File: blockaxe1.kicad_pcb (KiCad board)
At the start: 4 copper layers, 56.5 x 99.8 mm, 149 parts, among them J1 TC2030-IDC, J2 TC2030-IDC, J3 Conn_01x04, J4 USB_C_Receptacle_USB2.0, J5 PJ-002B, J6 Conn_01x04, J7 Conn_01x03, Q4 CSD17575Q3, Q5 CSD17312Q5, SW1 TL3330AF260QG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

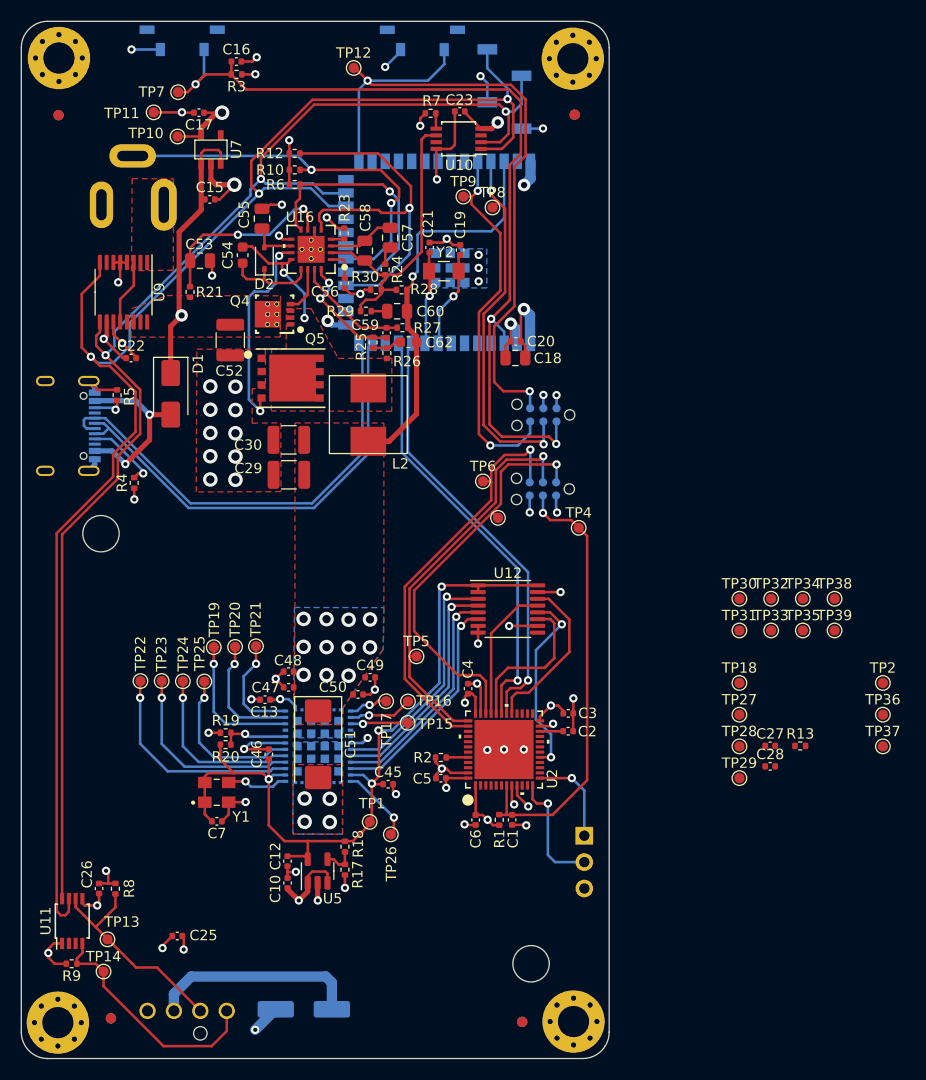
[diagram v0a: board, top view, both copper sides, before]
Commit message: switched barrel plug for #8. touched up schematic, DRC, generated BOM, generated Gerbers
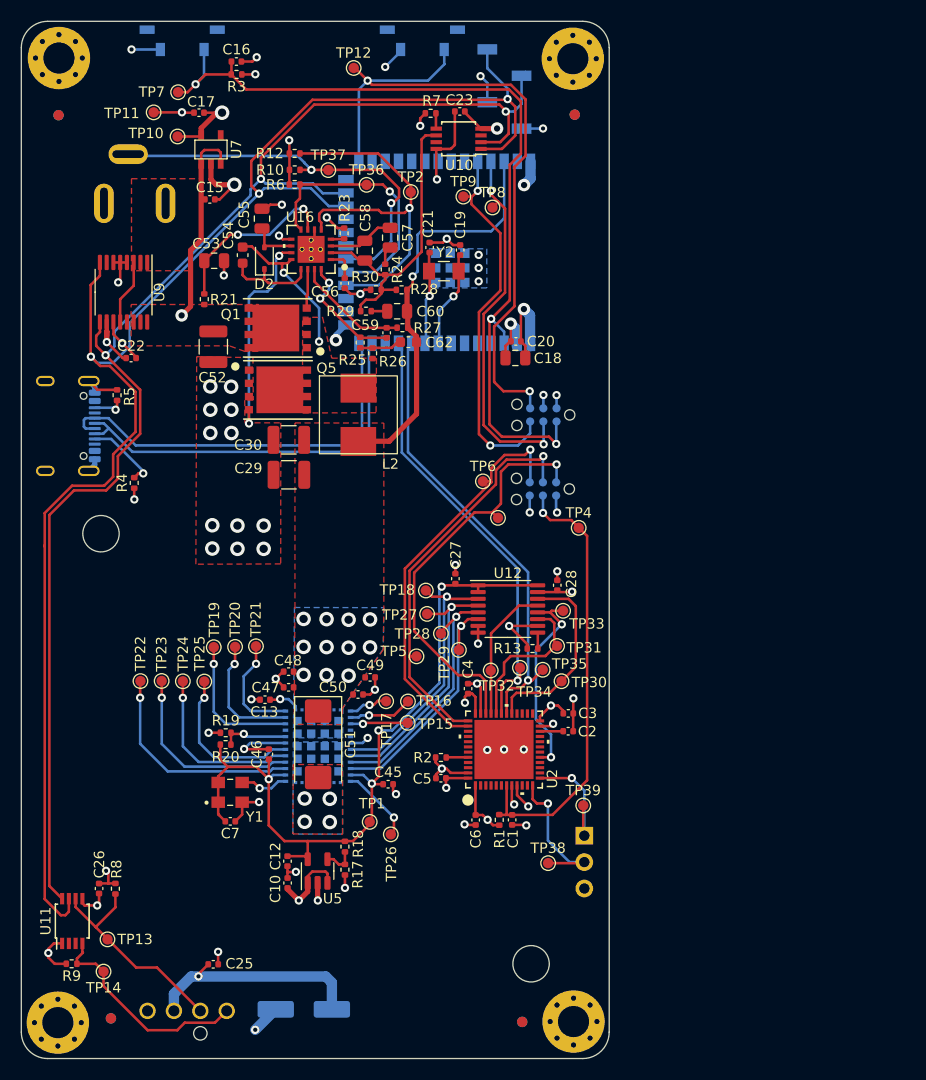
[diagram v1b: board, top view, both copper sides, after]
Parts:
- removed D1: SS310, Diode_SMD:D_SMA
- removed Q4: CSD17575Q3, blockaxe:DQG0008A
- added Q1: CSD17312Q5, blockaxe:DQH8, F.Cu at (128.4, 76.1)
- J5: value PJ-002B -> EJ503A; footprint blockaxe:CUI_PJ-002B -> blockaxe:MPD_EJ503A
- moved TP37 76.9 mm to (133.3, 61.0)
- moved TP36 71.2 mm to (136.9, 62.4)
- moved TP2 65.5 mm to (141.2, 63.1)
- moved TP38 37.5 mm to (154.4, 127.6)
- moved C27 34.3 mm to (145.5, 100.2), turned to 90 degrees
- moved TP27 31.6 mm to (142.8, 103.6)
- moved TP18 31.4 mm to (142.7, 101.4)
- moved TP28 30.7 mm to (144.1, 105.5)
- moved TP29 29.7 mm to (145.8, 107.1)
- moved TP39 29.5 mm to (157.8, 122.1)
- moved TP34 28.0 mm to (151.7, 108.8)
- moved TP32 27.8 mm to (148.9, 109.1)
- moved R13 27.4 mm to (152.9, 107.0)
- moved C28 26.9 mm to (155.3, 100.9), turned to 90 degrees
- moved TP35 25.3 mm to (153.9, 109.0)
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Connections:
- C10 pad 1: /3V3 -> VDD
- C17 pad 1: /3V3 -> VDD
- C18 pad 1: /3V3 -> VDD
- C20 pad 1: /3V3 -> VDD
- C22 pad 1: /3V3 -> VDD
- C23 pad 1: /3V3 -> VDD
- C26 pad 1: /3V3 -> VDD
- C28 pad 1: /3V3 -> VDD
- J2 pad 2: /3V3 -> VDD
- J3 pad 2: /3V3 -> VDD
- J4 pad A4: Net-(D1-Pad2) -> unconnected-(J4-VBUS-PadA4)
- J4 pad B4: Net-(D1-Pad2) -> unconnected-(J4-VBUS-PadB4)
- R10 pad 1: /3V3 -> VDD
- R12 pad 1: /3V3 -> VDD
- R3 pad 1: /3V3 -> VDD
- R6 pad 1: /3V3 -> VDD
- R8 pad 2: /3V3 -> VDD
- R9 pad 2: /3V3 -> VDD
- TP10 pad 1: /3V3 -> VDD
- U10 pad 8: /3V3 -> VDD
- U11 pad 1: /3V3 -> VDD
- U12 pad 15: /3V3 -> VDD
- U5 pad 1: /3V3 -> VDD
- U5 pad 3: /3V3 -> VDD
- U7 pad 5: /3V3 -> VDD
- U8 pad 15: /3V3 -> VDD
- U8 pad 2: /3V3 -> VDD
- U9 pad 10: /3V3 -> VDD
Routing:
- net VDD: track 20.0 -> 76.2 mm, vias 6 -> 19
- net /3V3: track 54.7 -> 0.00 mm, vias 13 -> 0
- net Net-(D1-Pad2): track 17.1 -> 0.00 mm, vias 2 -> 0
- net /5V: track 119.9 -> 113.7 mm
- net Net-(U8-GPIO20/U1CTS/ADC2_CH9/CLK_OUT1/USB_D+): track 44.7 -> 38.8 mm
- net Net-(U8-GPIO19/U1RTS/ADC2_CH8/CLK_OUT2/USB_D-): track 44.2 -> 38.6 mm
- net GND: track 142.8 -> 146.8 mm, vias 64 -> 68
- net /Power/SW: track 11.7 -> 14.7 mm
- net /STM32/RX2: track 9.10 -> 12.1 mm
- net /STM32/TRIP: track 15.9 -> 18.7 mm
- net /SCL: track 130.7 -> 133.5 mm
- net /STM32/TX2: track 11.7 -> 14.4 mm
- net /ASIC/TX_OUT: track 22.6 -> 25.2 mm
- net /Fan/FAN_PWM: track 23.3 -> 20.9 mm
- net /ASIC/RX_IN: track 21.7 -> 24.1 mm
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- added copper zone on In2.Cu, net VDD
- removed copper zone on In2.Cu, net /3V3
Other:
- board text added: "101"
- board text removed: "100"

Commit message: added stm32 crystal for #9
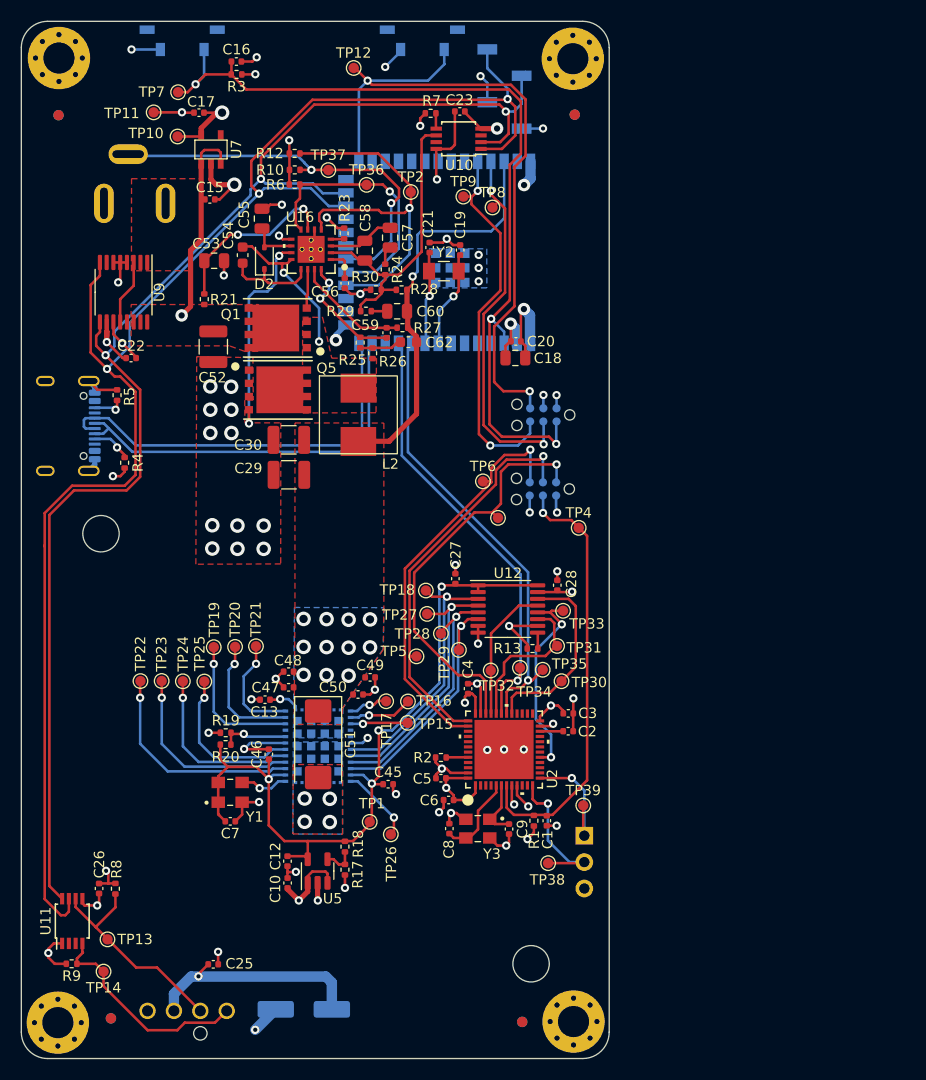
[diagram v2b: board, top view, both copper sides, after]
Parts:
- added C8: 20pF, Capacitor_SMD:C_0402_1005Metric, F.Cu at (144.9, 124.3)
- added C9: 20pF, Capacitor_SMD:C_0402_1005Metric, F.Cu at (150.7, 124.3)
- added Y3: 8MHz, blockaxe:XTAL_ECS-240-8-33-AGN-TR, F.Cu at (147.7, 124.3)
- moved C1 3.33 mm to (154.3, 123.5)
- moved R1 3.33 mm to (153.0, 123.5)
- moved C6 3.23 mm to (144.8, 121.5), turned to 180 degrees
- moved R4 2.15 mm to (113.7, 89.1)
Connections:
- SW1 pad 3: (no net) -> unconnected-(SW1-Pad3)
- SW1 pad 4: (no net) -> unconnected-(SW1-Pad4)
- SW2 pad 3: (no net) -> unconnected-(SW2-Pad3)
- SW2 pad 4: (no net) -> unconnected-(SW2-Pad4)
- U2 pad 5: unconnected-(U2-OSC_IN-Pad5) -> Net-(U2-OSC_IN)
- U2 pad 6: unconnected-(U2-OSC_OUT-Pad6) -> Net-(U2-OSC_OUT)
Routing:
- net Net-(U2-OSC_IN): track 0.00 -> 8.22 mm
- net GND: track 146.8 -> 153.1 mm, vias 68 -> 70
- net Net-(U2-OSC_OUT): track 0.00 -> 5.76 mm
- net Net-(J4-CC1): track 7.20 -> 3.87 mm
- net /SCL: track 133.5 -> 134.7 mm
- net /STM32/SWRESET: track 43.1 -> 42.0 mm
- net /SDA: track 151.3 -> 150.7 mm
- net VDD: track 76.2 -> 76.8 mm

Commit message: update to KiCad8, DNP 32kHz crystal
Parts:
- C27, C28: value 311-3342-1-ND -> 0.1uF
